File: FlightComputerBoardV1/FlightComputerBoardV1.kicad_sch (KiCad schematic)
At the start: 0 parts

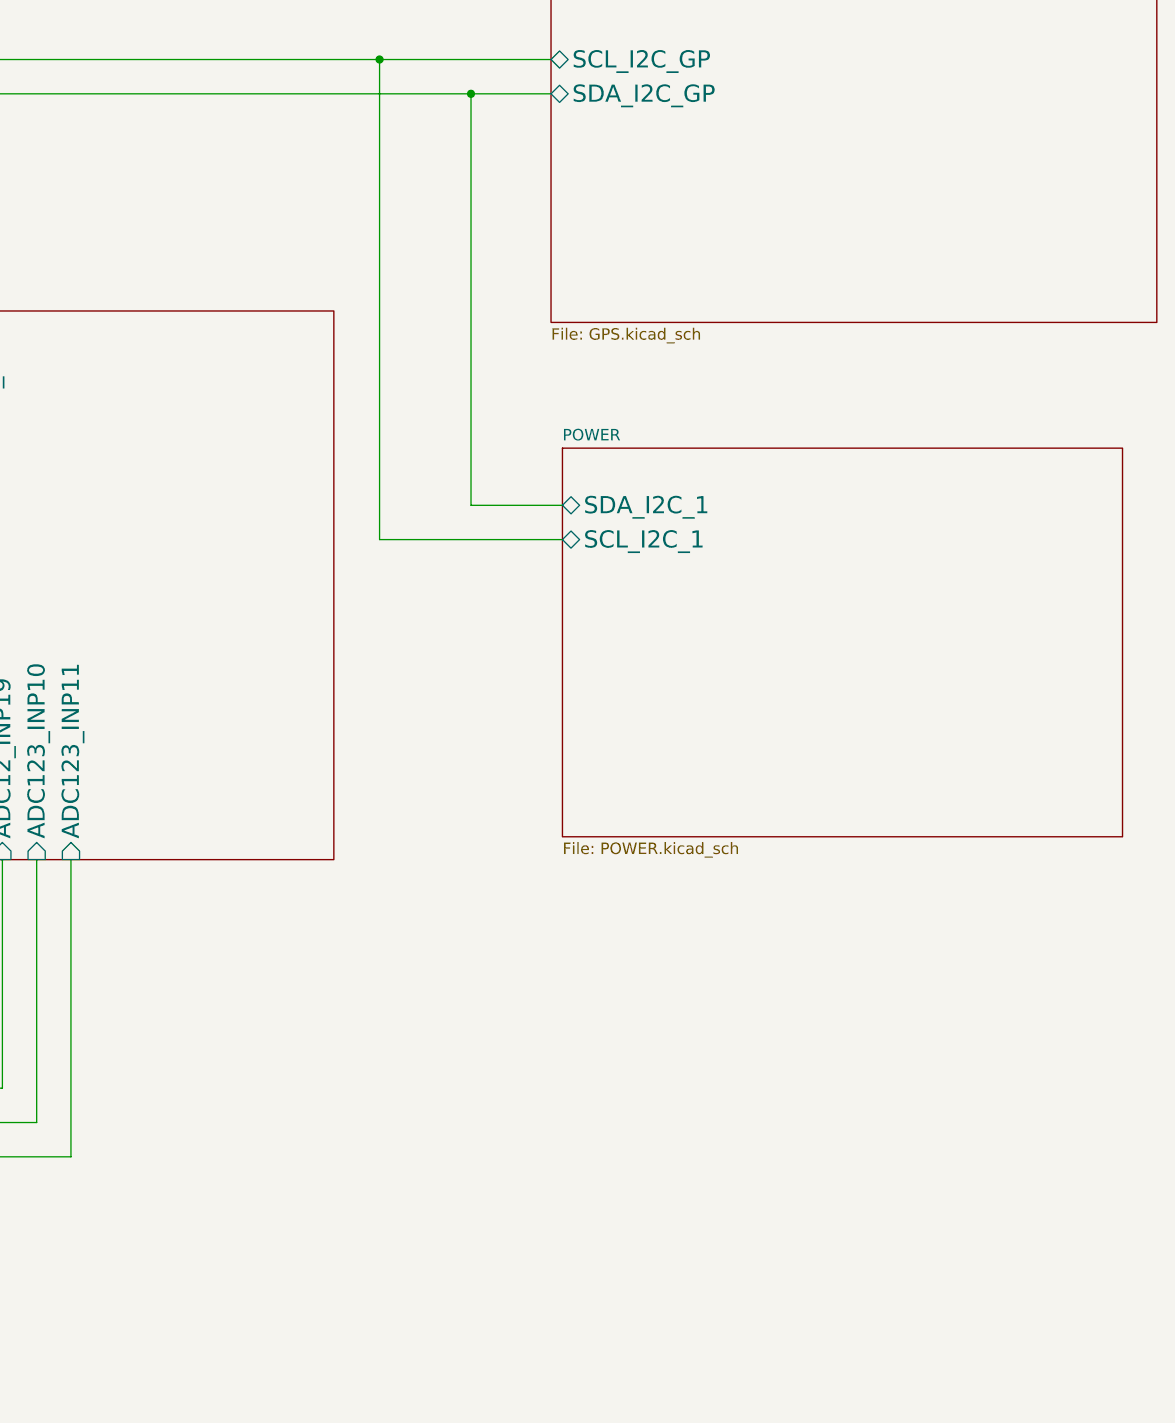
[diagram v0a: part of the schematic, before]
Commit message: Late night shenanigans
- Added radar module sheet
- Created symbols for: radar, RFD900xus
- Added RFD900xus
- Fixed PT voltage dividers
To do:
- Add decoupling and test points
- Finish finding appropriate gate driver for H bridge linear actuator circuit
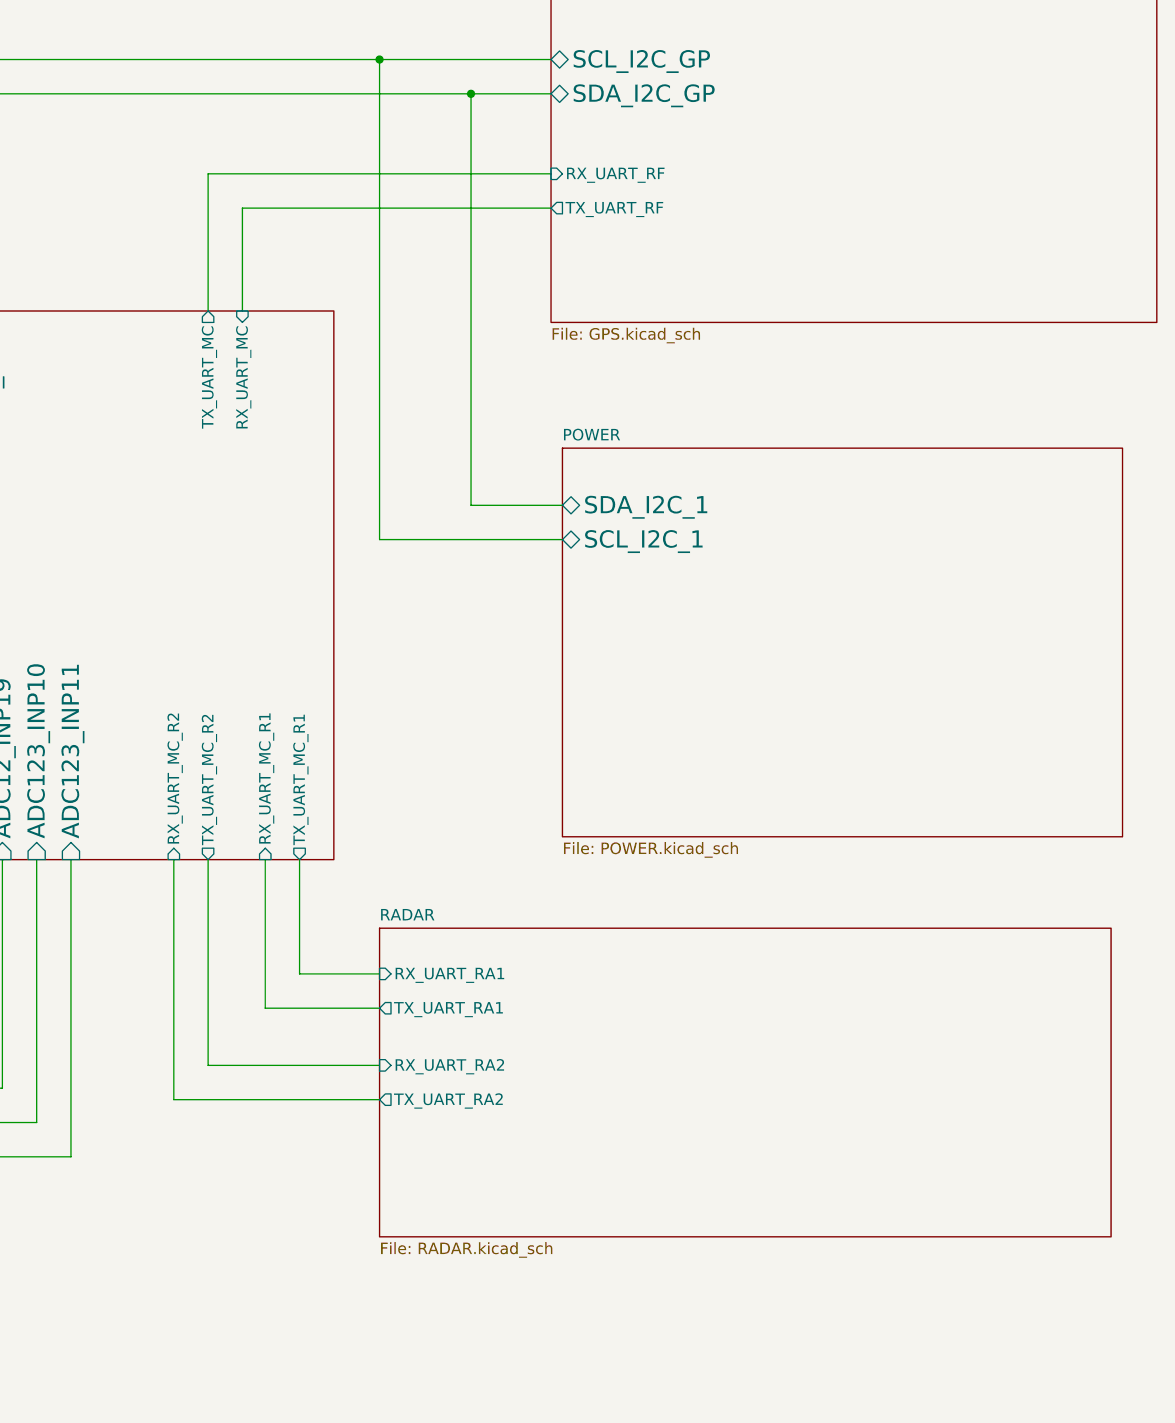
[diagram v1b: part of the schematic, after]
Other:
- added sheet RADAR (RADAR.kicad_sch)
- sheet GPS ports: added RX_UART_RF, TX_UART_RF; removed none
- sheet MCU ports: added RX_UART_MC, RX_UART_MC_R1, RX_UART_MC_R2, TX_UART_MC, TX_UART_MC_R1, TX_UART_MC_R2; removed none

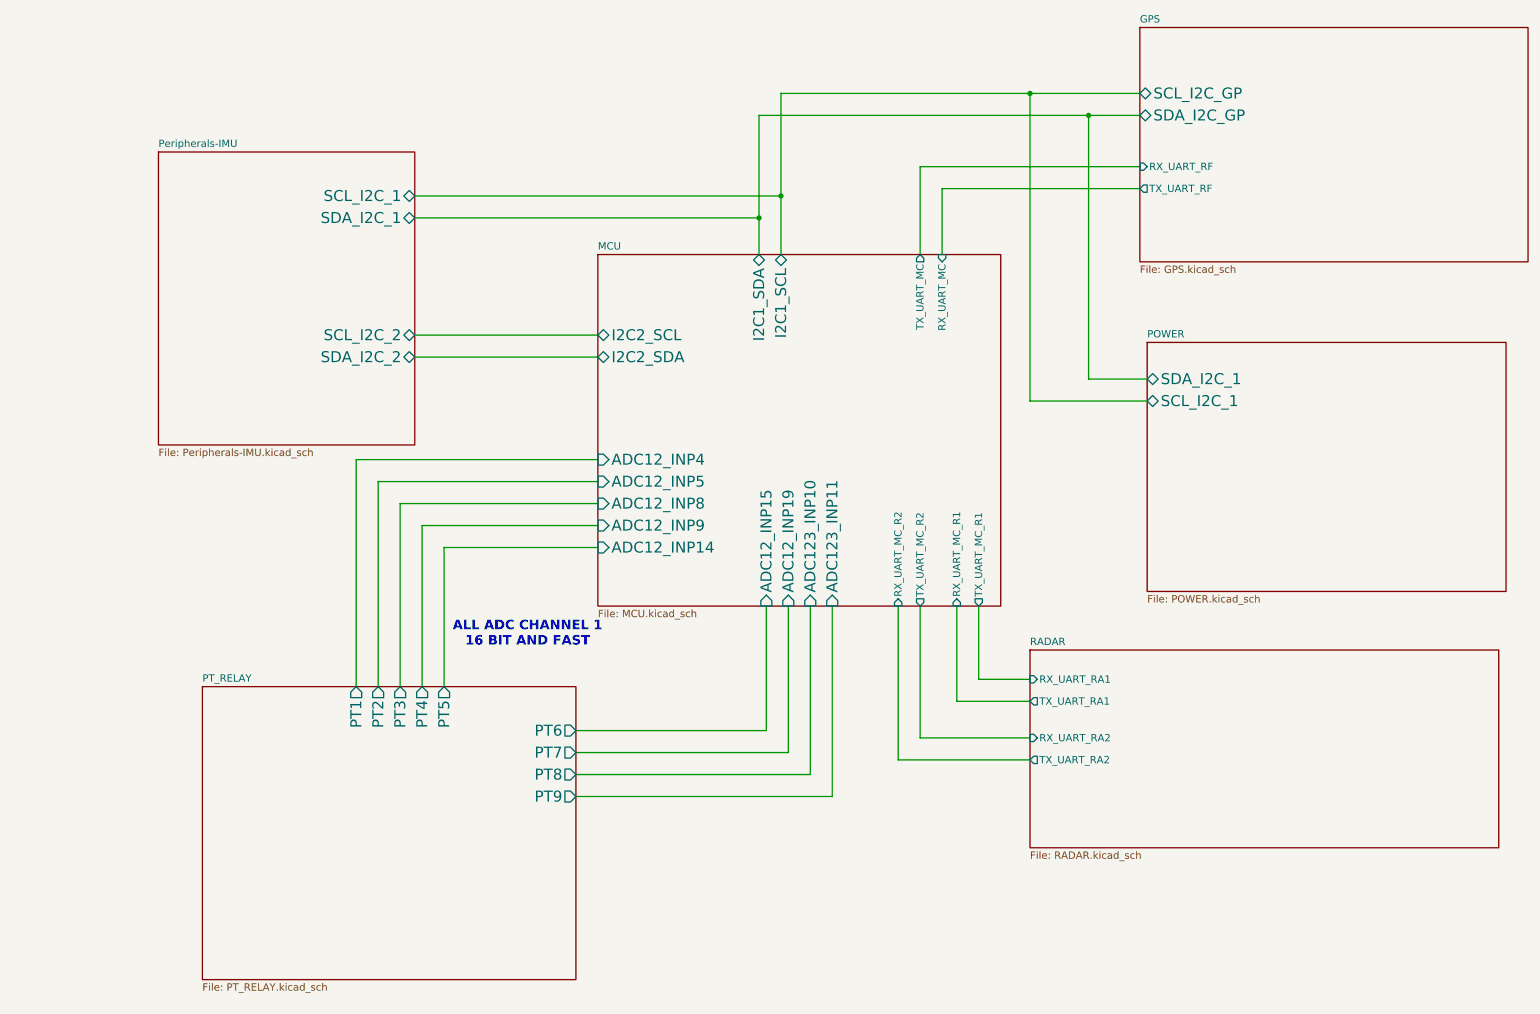
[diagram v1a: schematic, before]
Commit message: The Calamity
Design Changes:
- Swapped actuators to run on H bridge circuit
- Added potentiometer feedback for actuators
- Assigned pins for actuator control
- Added gate driver circuits
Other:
- Created very preliminary BOM (lifesucks.csv)
- Assigned most footprints

To do:
- Standardize component naming
- Finalize BOM (screw terminals once physical design starts)
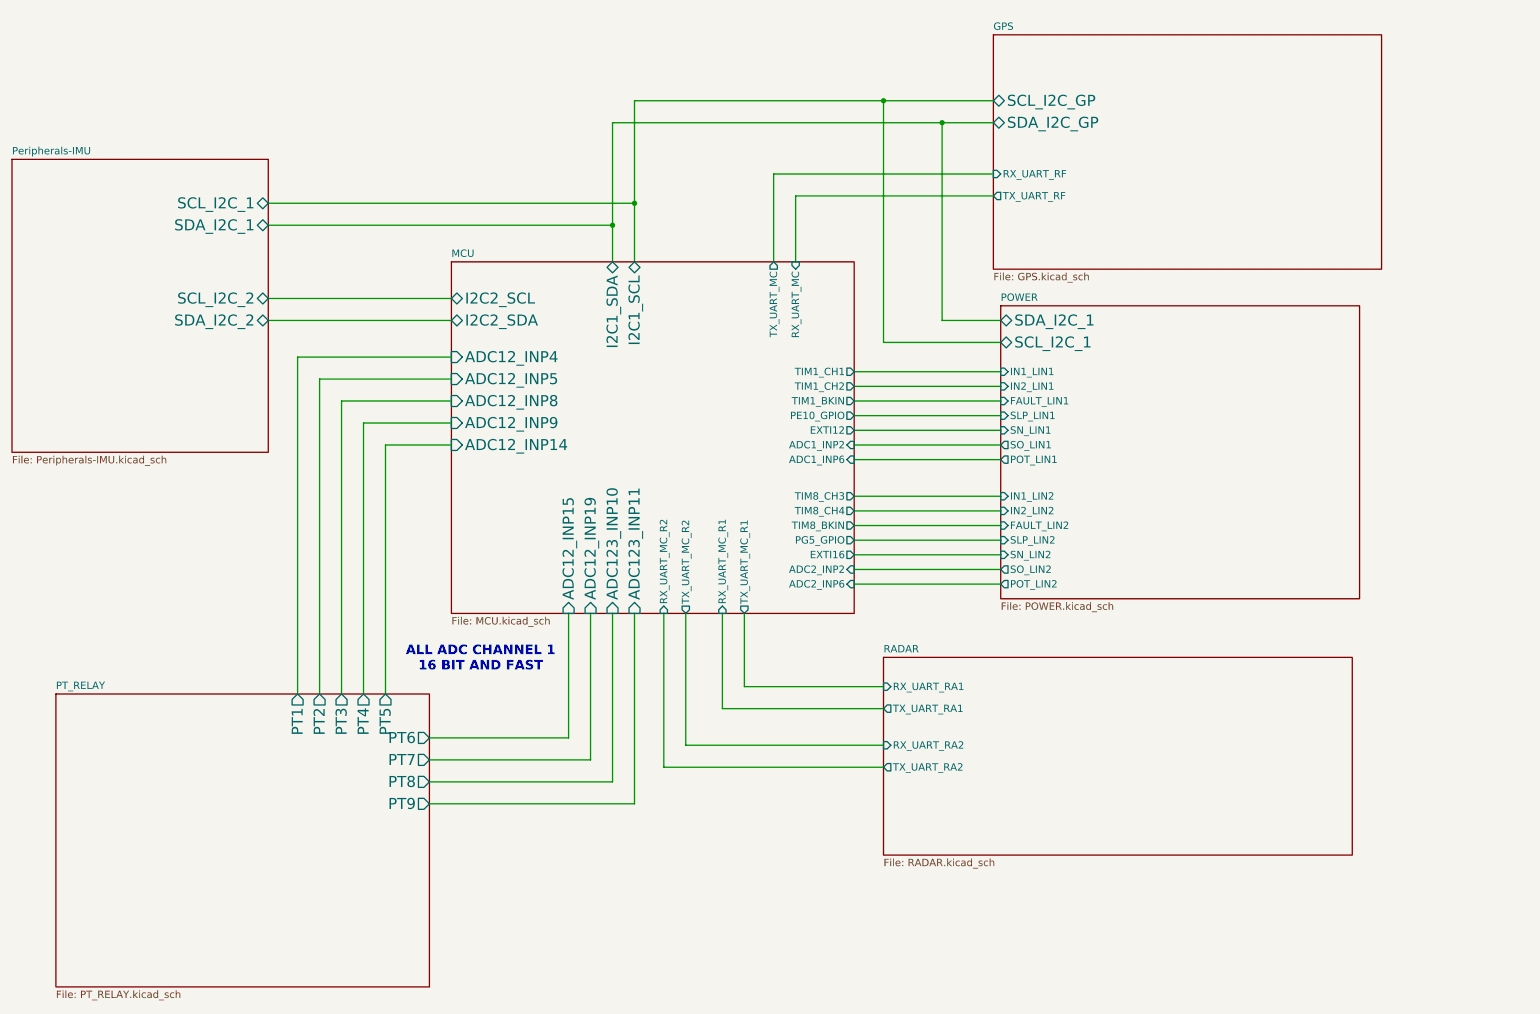
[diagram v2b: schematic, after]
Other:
- sheet MCU ports: added ADC1_INP2, ADC1_INP6, ADC2_INP2, ADC2_INP6, EXTI12, EXTI16, PE10_GPIO, PG5_GPIO, TIM1_BKIN, TIM1_CH1, TIM1_CH2, TIM8_BKIN, TIM8_CH3, TIM8_CH4; removed none
- sheet POWER ports: added FAULT_LIN1, FAULT_LIN2, IN1_LIN1, IN1_LIN2, IN2_LIN1, IN2_LIN2, POT_LIN1, POT_LIN2, SLP_LIN1, SLP_LIN2, SN_LIN1, SN_LIN2, SO_LIN1, SO_LIN2; removed none
